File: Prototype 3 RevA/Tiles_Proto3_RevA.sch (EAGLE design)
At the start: 27 parts, among them IC1 LSM9DS1, SW1 MF-SW-TACT-4.2MM, U1 RFD77101

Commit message: proto#3 schematics created
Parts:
- added H3, H4: MOUNT-PAD-ROUND2.8, holes:MOUNT-PAD-ROUND2.8
- added J1: (no value), SparkFun-Connectors:CONN_07
- added J2, J3: (no value), SparkFun-Connectors:CONN_041X04_NO_SILK
- added J4: (no value), tiles:CONN_041X04_NO_SILK
- added J5: (no value), tiles:CONN_04_SIM1X04_NO_SILK_ROUND
- H1, H2: value MOUNT-PAD-ROUND5.0 -> MOUNT-PAD-ROUND2.8; device holes:MOUNT-PAD-ROUND5.0 -> holes:MOUNT-PAD-ROUND2.8
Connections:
- removed net N$9: H2.MOUNT, U2.CS1
- new net GPIO16: J1.7, U1.P0.16
- net GND: now also J1.3
- net GPIO0(TX): now also J1.6
- net GPIO1(RX): now also J1.5
- net RESET: now also J1.1
- net VCC: now also J1.2
- net V_BATT: now also J1.4
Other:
- moved on the sheet: H1, H2, SW1
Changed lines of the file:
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@@
 <setting verticaltext="up"/>
 </settings>
-<grid distance="0.1" unitdist="inch" unit="inch" style="lines" multiple="1" display="no" altdistance="0.01" altunitdist="inch" altunit="inch"/>
+<grid distance="0.1" unitdist="inch" unit="inch" style="lines" multiple="1" display="yes" altdistance="0.01" altunitdist="inch" altunit="inch"/>
 <layers>
 <layer number="1" name="Top" color="4" fill="1" visible="no" active="no"/>
@@
 <part name="SW1" library="MF_Switches" deviceset="TACT" device="_4.2MM" value="MF-SW-TACT-4.2MM"/>
 <part name="U$20" library="microbuilder" deviceset="GND" device=""/>
-<part name="H1" library="holes" deviceset="MOUNT-PAD-ROUND" device="5.0"/>
-<part name="H2" library="holes" deviceset="MOUNT-PAD-ROUND" device="5.0"/>
 <part name="U$21" library="tiles" deviceset="9MBUZ" device=""/>
+<part name="J1" library="SparkFun-Connectors" deviceset="CONN_07" device=""/>
+<part name="H3" library="holes" deviceset="MOUNT-PAD-ROUND" device="2.8"/>
+<part name="H4" library="holes" deviceset="MOUNT-PAD-ROUND" device="2.8"/>
+<part name="H1" library="holes" deviceset="MOUNT-PAD-ROUND" device="2.8"/>
+<part name="H2" library="holes" deviceset="MOUNT-PAD-ROUND" device="2.8"/>
+<part name="J2" library="SparkFun-Connectors" deviceset="CONN_04" device="1X04_NO_SILK"/>
+<part name="J3" library="SparkFun-Connectors" deviceset="CONN_04" device="1X04_NO_SILK"/>
+<part name="J4" library="tiles" deviceset="CONN_04" device="1X04_NO_SILK"/>
+<part name="J5" library="tiles" deviceset="CONN_04_SIM" device="1X04_NO_SILK_ROUND"/>
 </parts>
 <sheets>
@@
 <instance part="P+11" gate="VCC" x="127" y="170.18"/>
 <instance part="U$19" gate="G$1" x="121.92" y="129.54"/>
-<instance part="SW1" gate="G$1" x="121.92" y="111.76" rot="R90"/>
-<instance part="U$20" gate="G$1" x="119.38" y="101.6"/>
-<instance part="H1" gate="G$1" x="167.64" y="91.44"/>
-<instance part="H2" gate="G$1" x="167.64" y="81.28"/>
+<instance part="SW1" gate="G$1" x="149.86" y="119.38" rot="R90"/>
+<instance part="U$20" gate="G$1" x="147.32" y="109.22"/>
 <instance part="U$21" gate="G$1" x="274.32" y="142.24"/>
+<instance part="J1" gate="G$1" x="210.82" y="121.92" rot="R180"/>
+<instance part="H3" gate="G$1" x="124.46" y="73.66" rot="R90"/>
+<instance part="H4" gate="G$1" x="134.62" y="73.66" rot="R90"/>
+<instance part="H1" gate="G$1" x="104.14" y="73.66" rot="R90"/>
+<instance part="H2" gate="G$1" x="114.3" y="73.66" rot="R90"/>
+<instance part="J2" gate="G$1" x="187.96" y="96.52" rot="R180"/>
+<instance part="J3" gate="G$1" x="187.96" y="73.66" rot="R180"/>
+<instance part="J4" gate="G$1" x="165.1" y="96.52" rot="R180"/>
+<instance part="J5" gate="G$1" x="165.1" y="73.66" rot="R180"/>
 </instances>
 <busses>
@@
 <pinref part="SW1" gate="G$1" pin="P$1"/>
 <pinref part="U$20" gate="G$1" pin="GND"/>
-<wire x1="119.38" y1="109.22" x2="119.38" y2="104.14" width="0.1524" layer="91"/>
+<wire x1="147.32" y1="116.84" x2="147.32" y2="111.76" width="0.1524" layer="91"/>
 </segment>
 <segment>
 <pinref part="U$21" gate="G$1" pin="BUZGND"/>
 <wire x1="172.72" y1="144.78" x2="187.96" y2="144.78" width="0.1524" layer="91"/>
+</segment>
+<segment>
+<pinref part="J1" gate="G$1" pin="3"/>
+<wire x1="187.96" y1="121.92" x2="205.74" y2="121.92" width="0.1524" layer="91"/>
+<label x="187.96" y="121.92" size="1.778" layer="95"/>
 </segment>
 </net>
@@
 <pinref part="D1" gate="G$1" pin="+"/>
 <wire x1="-10.16" y1="154.94" x2="-10.16" y2="147.32" width="0.1524" layer="91"/>
+</segment>
+<segment>
+<pinref part="J1" gate="G$1" pin="4"/>
+<wire x1="187.96" y1="119.38" x2="205.74" y2="119.38" width="0.1524" layer="91"/>
+<label x="187.96" y="119.38" size="1.778" layer="95"/>
 </segment>
 </net>
@@
 <wire x1="127" y1="167.64" x2="127" y2="162.56" width="0.1524" layer="91"/>
 </segment>
+<segment>
+<pinref part="J1" gate="G$1" pin="2"/>
+<wire x1="187.96" y1="124.46" x2="205.74" y2="124.46" width="0.1524" layer="91"/>
+<label x="187.96" y="124.46" size="1.778" layer="95"/>
+</segment>
 </net>
 <net name="RESET" class="0">
@@
 <label x="-2.54" y="129.54" size="1.778" layer="95"/>
 </segment>
+<segment>
+<pinref part="J1" gate="G$1" pin="1"/>
+<wire x1="187.96" y1="127" x2="205.74" y2="127" width="0.1524" layer="91"/>
+<label x="187.96" y="127" size="1.778" layer="95"/>
+</segment>
 </net>
 <net name="FACTORY" class="0">
@@
 <label x="43.18" y="71.12" size="1.778" layer="95" rot="R90"/>
 </segment>
+<segment>
+<pinref part="J1" gate="G$1" pin="6"/>
+<wire x1="187.96" y1="114.3" x2="205.74" y2="114.3" width="0.1524" layer="91"/>
+<label x="187.96" y="114.3" size="1.778" layer="95"/>
+</segment>
 </net>
 <net name="GPIO1(RX)" class="0">
@@
 <wire x1="38.1" y1="83.82" x2="38.1" y2="68.58" width="0.1524" layer="91"/>
 <label x="38.1" y="71.12" size="1.778" layer="95" rot="R90"/>
+</segment>
+<segment>
+<pinref part="J1" gate="G$1" pin="5"/>
+<wire x1="187.96" y1="116.84" x2="205.74" y2="116.84" width="0.1524" layer="91"/>
+<label x="187.96" y="116.84" size="1.778" layer="95"/>
 </segment>
 </net>
@@
 <segment>
 <pinref part="SW1" gate="G$1" pin="P$3"/>
-<wire x1="124.46" y1="109.22" x2="124.46" y2="104.14" width="0.1524" layer="91"/>
-<wire x1="124.46" y1="104.14" x2="139.7" y2="104.14" width="0.1524" layer="91"/>
-<label x="129.54" y="104.14" size="1.778" layer="95"/>
+<wire x1="152.4" y1="116.84" x2="152.4" y2="111.76" width="0.1524" layer="91"/>
+<wire x1="152.4" y1="111.76" x2="167.64" y2="111.76" width="0.1524" layer="91"/>
+<label x="157.48" y="111.76" size="1.778" layer="95"/>
 </segment>
 </net>
@@
 </segment>
 </net>
-<net name="N$9" class="0">
-<segment>
-<pinref part="U2" gate="G$1" pin="CS1"/>
-<wire x1="147.32" y1="48.26" x2="154.94" y2="48.26" width="0.1524" layer="91"/>
-<wire x1="154.94" y1="48.26" x2="154.94" y2="81.28" width="0.1524" layer="91"/>
-<pinref part="H2" gate="G$1" pin="MOUNT"/>
-<wire x1="154.94" y1="81.28" x2="165.1" y2="81.28" width="0.1524" layer="91"/>
-</segment>
-</net>
+<net name="GPIO16" class="0">
+<segment>
+<pinref part="U1" gate="G$1" pin="P0.16"/>
+<wire x1="-2.54" y1="114.3" x2="10.16" y2="114.3" width="0.1524" layer="91"/>
+<label x="-2.54" y="114.3" size="1.778" layer="95"/>
+</segment>
+<segment>
+<pinref part="J1" gate="G$1" pin="7"/>
+<wire x1="187.96" y1="111.76" x2="205.74" y2="111.76" width="0.1524" layer="91"/>
+<label x="187.96" y="111.76" size="1.778" layer="95"/>
+</segment>
+</net>

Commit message: routing finshed
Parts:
- removed BAT+, BAT-: (no value), wirepad:SMD2
- removed H1, H2, H3, H4: MOUNT-PAD-ROUND2.8, holes:MOUNT-PAD-ROUND2.8
- removed J2, J3: (no value), SparkFun-Connectors:CONN_041X04_NO_SILK
- removed J4: (no value), tiles:CONN_041X04_NO_SILK
- removed J5: (no value), tiles:CONN_04_SIM1X04_NO_SILK_ROUND
- removed SW1: MF-SW-TACT-4.2MM, MF_Switches:TACT_4.2MM
- removed U$21: 9MBUZ, tiles:9MBUZ
- added B+, B-: (no value), wirepad:1,6/0,8
- added BATT1: BAT-HLD-001, tiles:BATTERY-SMALL_BAT-HLD-001
- added BT1: (no value), SparkFun-Batteries:BATTERY-12MM_SMD
- added BT2: (no value), SparkFun-Batteries:BATTERY-20MM_SMD
- added CAP: (no value), SparkFun-Connectors:CONN_021X02_NO_SILK
- added CAP-A, CAP-B, IO-2, IO-3: MOUNT-PAD-ROUND2.5, tiles:MOUNT-PAD-ROUND2.5
- added D2: MF-LED-0603-RED, MF_LEDs:LED_SINGLE-0603-RED
- added GROVE-GPIO: (no value), SparkFun-Connectors:CONN_041X04_NO_SILK
- added GROVE-I2C: (no value), tiles:CONN_04_SIM1X04_NO_SILK
- added HAPTIC: DRV2605L, SparkFun-IC-Special-Function:DRV2605L
- added JP1: JUMPER-SMT_2_NO_NO-SILK, SparkFun-Jumpers:JUMPER-SMT_2_NO_NO-SILK
- added R6: 330, MF_Passives:RESISTOR_0603
- added R7: 10K 1/10W, Seeed-OPL-Resistor:SMD-RES-10K-5%-1/10W(0603)
- added R8: 1K 1/10W, Seeed-OPL-Resistor:SMD-RES-10K-5%-1/10W(0603)
- added SW2: MF-SW-TACT-4.2MM, MF_Switches:TACT_4.2MM
- added TOUCH: (no value), cap1188-microbuilder:CAP1188
- C1: value 10uf -> 1uf
- J1: device SparkFun-Connectors:CONN_07 -> tiles:CONN_07_SIMNO_SILK
- M+, M-: device wirepad:SMD2 -> wirepad:1,6/0,8
- U$1: value DRV2605L -> 4MBUZ; device SparkFun-IC-Special-Function:DRV2605L -> tiles:4MBUZ
- U2: value (none) -> MF-DSC-SOT233-MMBT3904; device cap1188-microbuilder:CAP1188 -> MF_Discrete_Semiconductor:NPN_BJTMMBT3904_SOT-23-3
- renumbered IC1 to IMU
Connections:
- removed net CAPINT: R3.1, U1.P0.30, U2.ALERT#/BC_IRQ#
- removed net CAPRES: R4.2, U1.P0.29, U2.RESET
- removed net GPIO16: J1.7, U1.P0.16
- new net BTN: SW2.P$3, U1.P0.16
- new net CAP-A: CAP-A.MOUNT, CAP.1, TOUCH.CS1
- new net CAP-B: CAP-B.MOUNT, CAP.2, TOUCH.CS2
- new net CAP-INT: R3.1, TOUCH.ALERT#/BC_IRQ#, U1.P0.15
- new net CAP-RES: R4.2, TOUCH.RESET, U1.P0.12
- new net IMU-INT: IMU.INT1_A/G, U1.P0.08
- new net IO-2: GROVE-GPIO.1, IO-2.MOUNT, J1.7, U1.P0.02/AIN3
- new net IO-3: GROVE-GPIO.2, IO-3.MOUNT, U1.P0.03/AIN4
- new net N$10: IMU.INT_M
- new net N$12: IMU.INT2_A/G
- new net N$9: D2.ANODE, R6.P$2
- net BUZZER: now also R7.2, U1.P0.07, U2.BASE; no longer U$21.BUZSIG, U1.P0.18
- net GND: now also B-.P, BATT1.NEG, C5.2, C7.1, D2.CATHODE, GROVE-GPIO.4, GROVE-I2C.1, HAPTIC.GND, R7.1, SW2.P$1, TOUCH.SPI_CS, TOUCH.THERMAL/GND, U2.EMITTER; no longer BAT-.P, SW1.P$1, U$1.GND, U$21.BUZGND, U2.THERMAL/GND
- net N$3: now also TOUCH.ADDR_COMM; no longer U2.ADDR_COMM
- net N$4: now also R8.1, U$1.BUZGND, U2.COLLECTOR; no longer C5.2, U2.VDD
- net N$5: now also HAPTIC.REG; no longer U$1.REG
- net N$6: now also J1.4, JP1.2; no longer C7.1, U$1.EN, U$1.VDD, U$1.VDD/NC
- net N$7: now also HAPTIC.OUT-; no longer U$1.OUT-
- net N$8: now also HAPTIC.OUT+; no longer U$1.OUT+
- net NEOPIX: now also U1.P0.09; no longer U1.P0.19
- net PWRBTN: no longer SW1.P$3
- net SCL: now also GROVE-I2C.4, HAPTIC.SCL, TOUCH.SMCLK/BC_CLK/SPI_CLK; no longer U$1.SCL, U2.SMCLK/BC_CLK/SPI_CLK
- net SDA: now also GROVE-I2C.3, HAPTIC.SDA, TOUCH.SMDATA/BC_DATA/SPI_MISO; no longer U$1.SDA, U2.SMDATA/BC_DATA/SPI_MISO
- net STATLED: now also R6.P$1
- net VCC: now also GROVE-GPIO.3, GROVE-I2C.2, HAPTIC.EN, HAPTIC.VDD, HAPTIC.VDD/NC, R8.2, TOUCH.VDD, U$1.BUZSIG+
- net V_BATT: now also B+.P, BATT1.POS, JP1.1; no longer BAT+.P, J1.4
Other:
- moved on the sheet: C2, C5, C7, C8, J1

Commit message: finished cleanup
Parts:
- removed BT1: (no value), SparkFun-Batteries:BATTERY-12MM_SMD
- removed BT2: (no value), SparkFun-Batteries:BATTERY-20MM_SMD
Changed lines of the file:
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@@
 <part name="SUPPLY2" library="SparkFun-PowerSymbols" deviceset="V_BATT" device=""/>
 <part name="U$27" library="microbuilder" deviceset="GND" device=""/>
-<part name="BT1" library="SparkFun-Batteries" deviceset="BATTERY" device="-12MM_SMD"/>
-<part name="BT2" library="SparkFun-Batteries" deviceset="BATTERY" device="-20MM_SMD"/>
 </parts>
 <sheets>
@@
 <instance part="SUPPLY2" gate="G$1" x="35.56" y="160.02" rot="R90"/>
 <instance part="U$27" gate="G$1" x="73.66" y="160.02" rot="R90"/>
-<instance part="BT1" gate="G$1" x="134.62" y="81.28"/>
-<instance part="BT2" gate="G$1" x="106.68" y="81.28"/>
 </instances>
 <busses>

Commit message: added text
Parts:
- CAP: device SparkFun-Connectors:CONN_021X02_NO_SILK -> cap1188-microbuilder:CAP1188
- TOUCH: device cap1188-microbuilder:CAP1188 -> SparkFun-Connectors:CONN_021X02_NO_SILK
- renumbered D2 to STAT, GROVE-GPIO to GPIO, GROVE-I2C to I2C, LED1 to LED, SW2 to SW, U$1 to BUZZER, U1 to SIMBLEE
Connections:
- net CAP-A: now also CAP.CS1, TOUCH.1; no longer CAP.1, TOUCH.CS1
- net CAP-B: now also CAP.CS2, TOUCH.2; no longer CAP.2, TOUCH.CS2
- net CAP-INT: now also CAP.ALERT#/BC_IRQ#; no longer TOUCH.ALERT#/BC_IRQ#
- net CAP-RES: now also CAP.RESET; no longer TOUCH.RESET
- net GND: now also CAP.SPI_CS, CAP.THERMAL/GND; no longer TOUCH.SPI_CS, TOUCH.THERMAL/GND
- net N$3: now also CAP.ADDR_COMM; no longer TOUCH.ADDR_COMM
- net SCL: now also CAP.SMCLK/BC_CLK/SPI_CLK; no longer TOUCH.SMCLK/BC_CLK/SPI_CLK
- net SDA: now also CAP.SMDATA/BC_DATA/SPI_MISO; no longer TOUCH.SMDATA/BC_DATA/SPI_MISO
- net VCC: now also CAP.VDD; no longer TOUCH.VDD

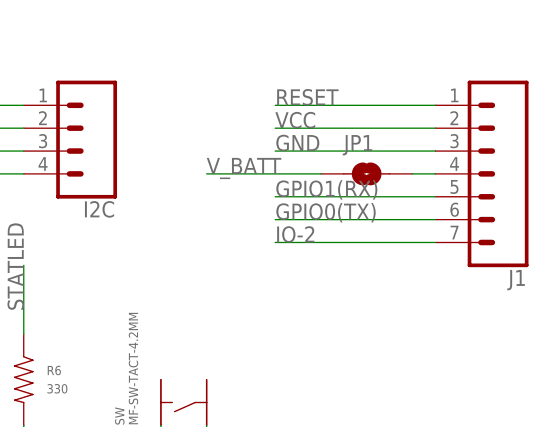
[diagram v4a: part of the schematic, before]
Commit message: finished silkscreen
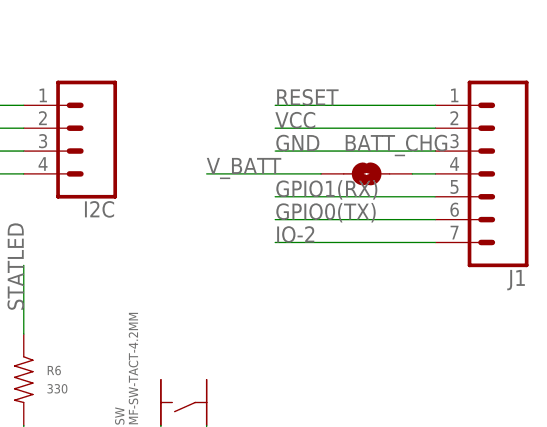
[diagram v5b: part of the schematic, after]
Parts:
- renumbered JP1 to BATT_CHG
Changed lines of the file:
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@@
 </part>
 <part name="BATT1" library="tiles" deviceset="BATTERY-SMALL" device="_BAT-HLD-001" value="BAT-HLD-001"/>
-<part name="JP1" library="SparkFun-Jumpers" deviceset="JUMPER-SMT_2_NO" device="_NO-SILK"/>
+<part name="BATT_CHG" library="SparkFun-Jumpers" deviceset="JUMPER-SMT_2_NO" device="_NO-SILK"/>
 <part name="SUPPLY2" library="SparkFun-PowerSymbols" deviceset="V_BATT" device=""/>
 <part name="U$27" library="microbuilder" deviceset="GND" device=""/>
@@
 <instance part="R8" gate="G$1" x="218.44" y="96.774" rot="R90"/>
 <instance part="BATT1" gate="G$1" x="50.8" y="160.02" rot="R90"/>
-<instance part="JP1" gate="G$1" x="220.98" y="157.48" smashed="yes">
+<instance part="BATT_CHG" gate="G$1" x="220.98" y="157.48" smashed="yes">
 <attribute name="NAME" x="218.44" y="160.02" size="1.778" layer="95" font="vector"/>
 </instance>
@@
 </segment>
 <segment>
-<pinref part="JP1" gate="G$1" pin="1"/>
+<pinref part="BATT_CHG" gate="G$1" pin="1"/>
 <wire x1="215.9" y1="157.48" x2="203.2" y2="157.48" width="0.1524" layer="91"/>
 <label x="203.2" y="157.48" size="1.778" layer="95"/>
@@
 <net name="N$6" class="0">
 <segment>
-<pinref part="JP1" gate="G$1" pin="2"/>
+<pinref part="BATT_CHG" gate="G$1" pin="2"/>
 <pinref part="J1" gate="G$1" pin="4"/>
 <wire x1="226.06" y1="157.48" x2="228.6" y2="157.48" width="0.1524" layer="91"/>

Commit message: added tiles dock
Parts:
- J1: device tiles:CONN_07_SIMNO_SILK -> tiles:CONN_07_SIMSQPAD_BOTTOM
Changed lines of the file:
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@@
 <part name="P+11" library="microbuilder" deviceset="VCC" device=""/>
 <part name="U$19" library="microbuilder" deviceset="GND" device=""/>
-<part name="J1" library="tiles" deviceset="CONN_07_SIM" device="NO_SILK"/>
+<part name="J1" library="tiles" deviceset="CONN_07_SIM" device="SQPAD_BOTTOM"/>
 <part name="IO-2" library="tiles" deviceset="MOUNT-PAD-ROUND" device="2.5"/>
 <part name="IO-3" library="tiles" deviceset="MOUNT-PAD-ROUND" device="2.5"/>

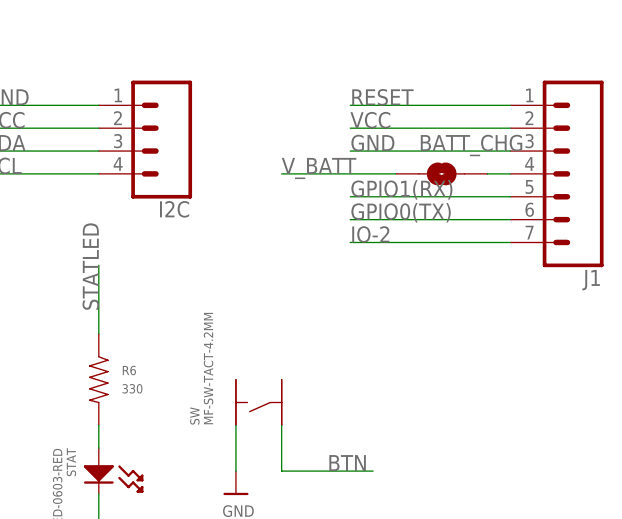
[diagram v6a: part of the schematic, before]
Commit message: increased holes to 3mm
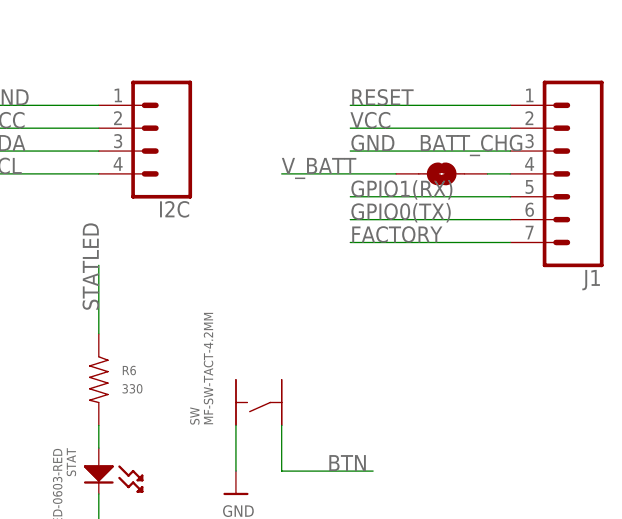
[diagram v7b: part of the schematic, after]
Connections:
- net FACTORY: now also J1.7
- net IO-2: no longer J1.7
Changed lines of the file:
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@@
 <label x="-2.54" y="127" size="1.778" layer="95"/>
+</segment>
+<segment>
+<pinref part="J1" gate="G$1" pin="7"/>
+<wire x1="210.82" y1="149.86" x2="228.6" y2="149.86" width="0.1524" layer="91"/>
+<label x="210.82" y="149.86" size="1.778" layer="95"/>
 </segment>
 </net>
@@
 <label x="142.24" y="101.6" size="1.778" layer="95"/>
 </segment>
-<segment>
-<pinref part="J1" gate="G$1" pin="7"/>
-<wire x1="210.82" y1="149.86" x2="228.6" y2="149.86" width="0.1524" layer="91"/>
-<label x="210.82" y="149.86" size="1.778" layer="95"/>
-</segment>
-</net>
+</net>
